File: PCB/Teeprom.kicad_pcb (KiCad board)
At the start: 2 copper layers, 38 x 16.6 mm, 3 parts, among them J1 Tandy_100_102_200_option_rom, U1 28C256 / FM18W08

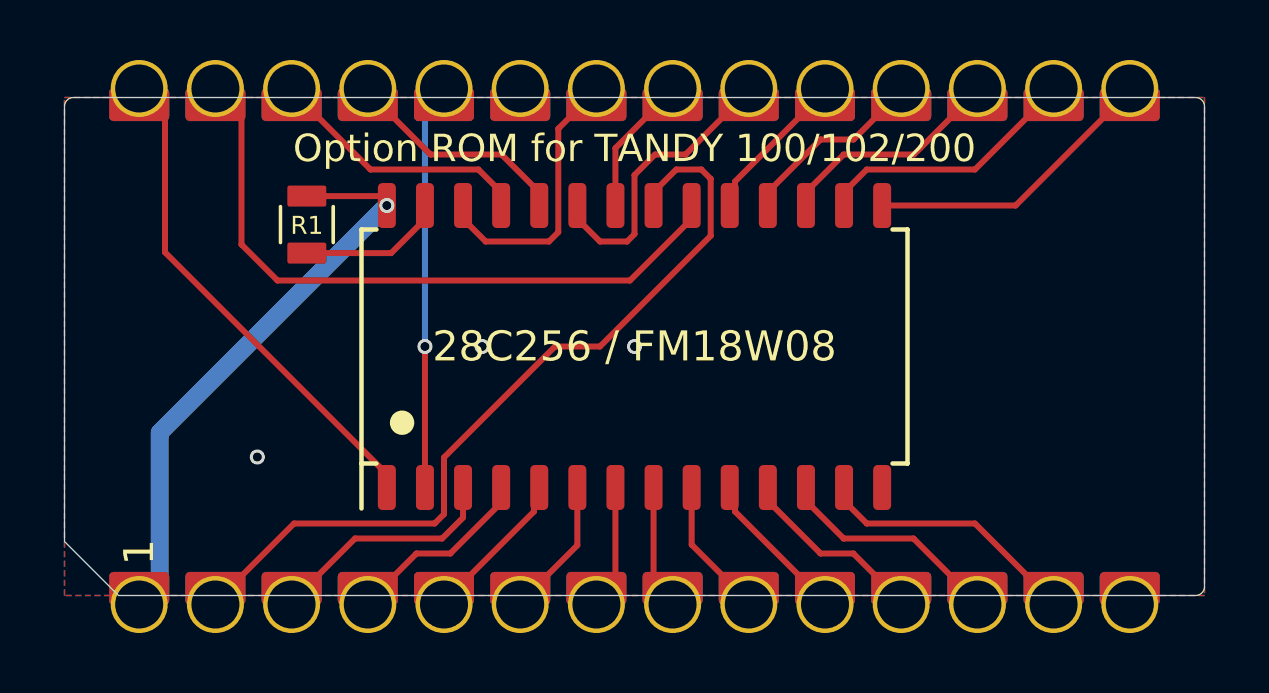
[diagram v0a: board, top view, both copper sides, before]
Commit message: add caps & fiducials, remove dead shapeways links
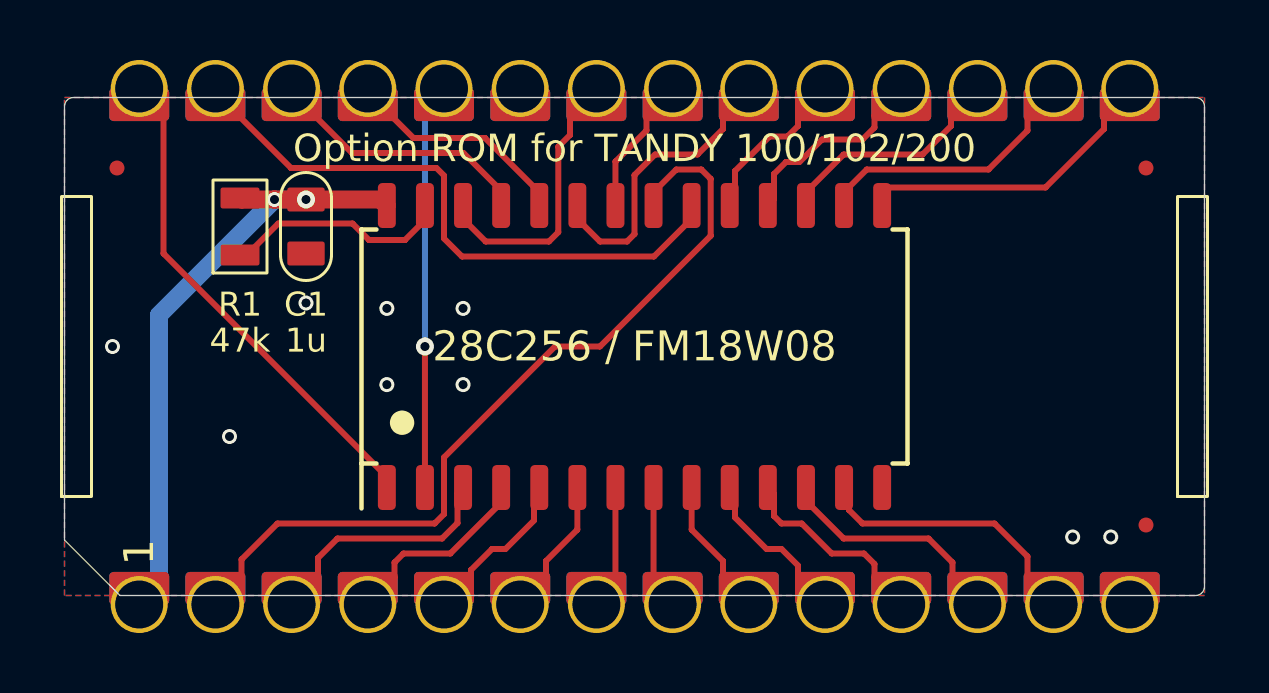
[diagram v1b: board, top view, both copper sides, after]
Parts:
- added C1: 1u, 000_LOCAL:C_0805, F.Cu at (136.3, 95.2)
- added N1: Molex78802_PCB_28_Carrier, 000_LOCAL:Molex78802_PCB_28_Carrier, F.Cu at (147.2, 99.2)
- added REF**: Fiducial_0.5mm_Mask1mm, 000_LOCAL:Fiducial_0.5mm_Mask1mm, F.Cu at (164.3, 105.1)
- added REF**: Fiducial_0.5mm_Mask1mm, 000_LOCAL:Fiducial_0.5mm_Mask1mm, F.Cu at (130.0, 93.2)
- added REF**: Fiducial_0.5mm_Mask1mm, 000_LOCAL:Fiducial_0.5mm_Mask1mm, F.Cu at (164.3, 93.2)
- moved R1 2.23 mm to (134.1, 95.2)
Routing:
- net /~{WE}: track 4.86 -> 7.59 mm
- net /~{CE}: track 22.4 -> 20.5 mm
- net VCC: track 19.7 -> 21.4 mm, vias 1 -> 2
- net /D3: track 9.93 -> 10.5 mm
- net GND: vias 3 -> 9
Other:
- board text added: "R1: 10k - 100k C1: 0.1u - 1u Carrier: ${0ecf4f0a-134a-478f-9aae-08160c56e454:VALUE}"
- board text removed: "R1: ${00000000-0000-0000-0000-00005d22c129:VALUE} ${COMMENT4}"
